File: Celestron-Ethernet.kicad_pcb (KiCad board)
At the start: 4 copper layers, 88.9 x 31.8 mm, 69 parts, among them J1 Joystick, J2 GPS, J3 6P6C, J4 RJ45_Amphenol_RJMG1BD3B8K1ANR, SW1 SW_DIP_x02, SW2 SW_Push, U1 74AHC1G125, U2 ATmega328P-AU, U3 NCV33375ST-3.3, U4 W5500, Y1 8MHz, Y2 25MHz

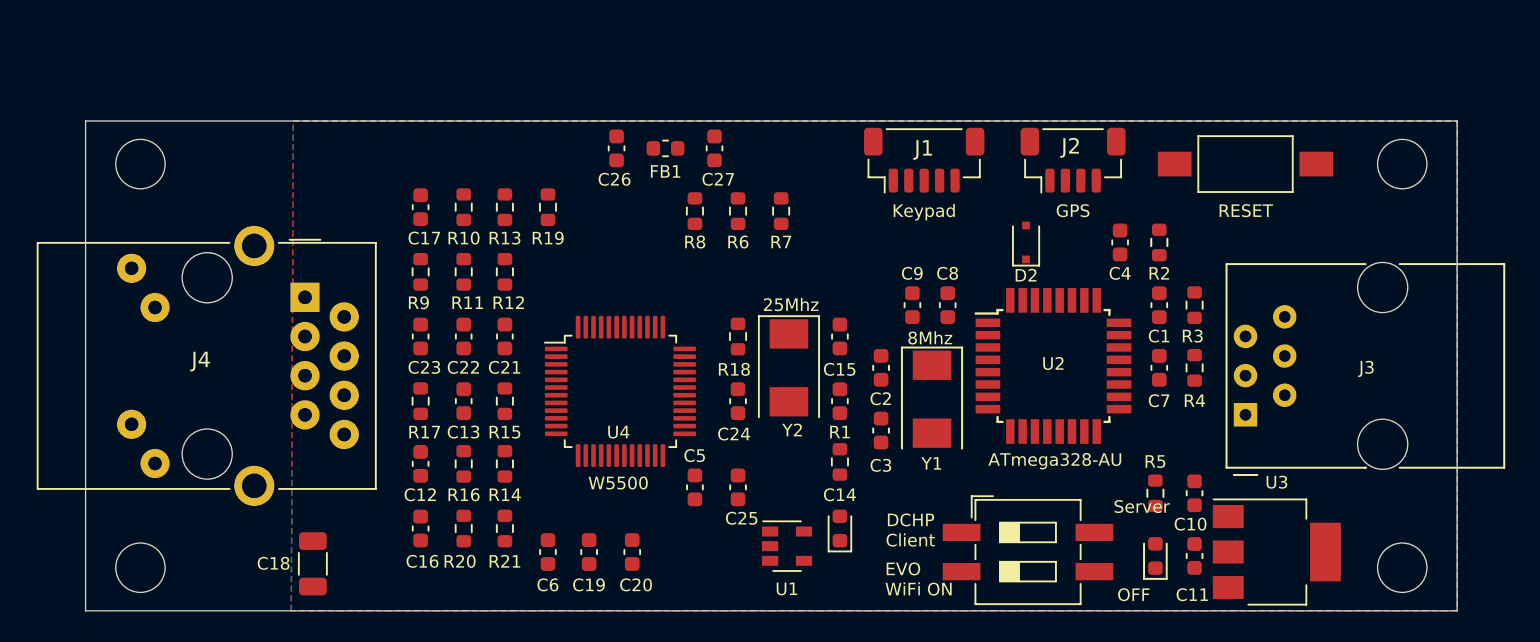
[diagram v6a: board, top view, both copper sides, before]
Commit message: grid spacing
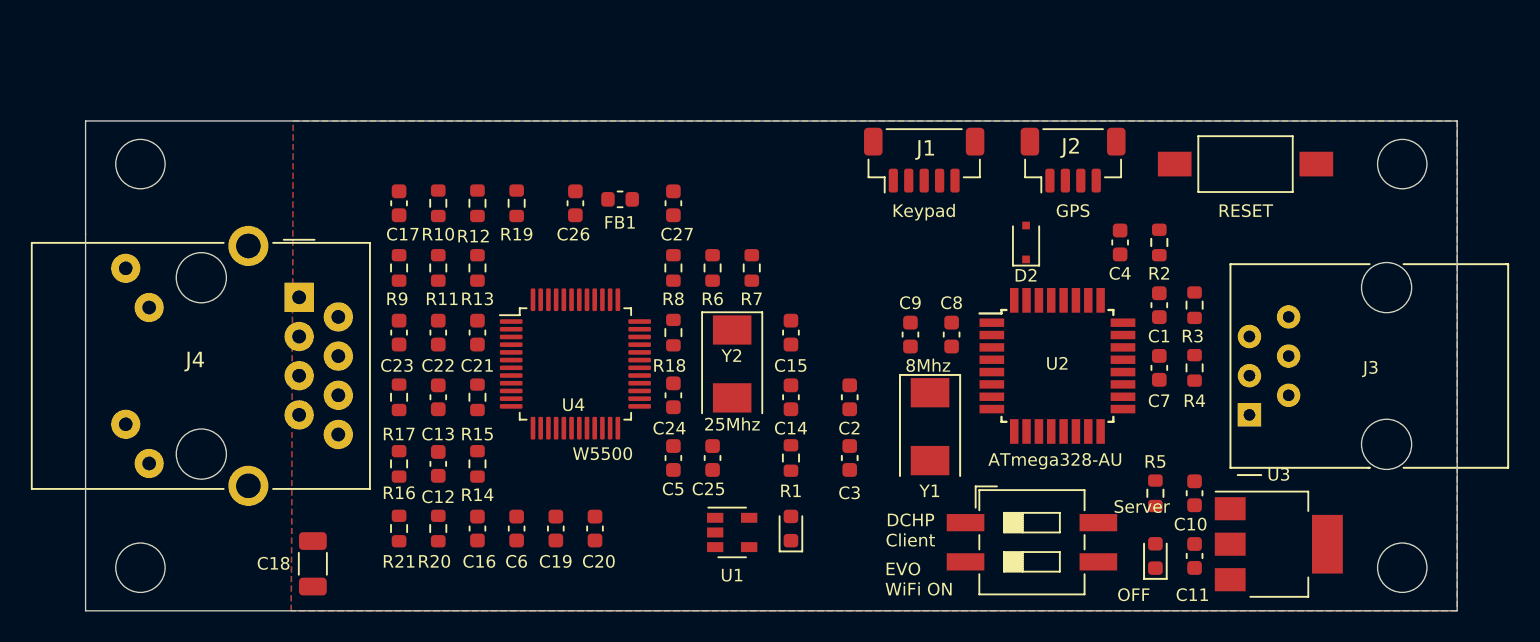
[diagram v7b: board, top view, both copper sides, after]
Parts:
- moved R21 6.86 mm to (121.9, 109.0)
- moved C26 4.44 mm to (133.3, 87.9)
- moved C27 4.44 mm to (139.7, 87.9)
- moved FB1 4.43 mm to (136.2, 87.6)
- moved C24 4.21 mm to (139.7, 100.3)
- moved R18 4.20 mm to (139.7, 96.3)
- moved R16 4.19 mm to (121.9, 104.8), turned to 90 degrees
- moved R7 4.15 mm to (144.8, 92.1)
- moved R6 4.04 mm to (142.2, 92.1)
- moved R8 3.94 mm to (139.7, 92.1)
- moved Y2 3.69 mm to (143.5, 98.3)
- moved C16 3.68 mm to (127.0, 109.0)
- moved U1 3.67 mm to (143.5, 109.2)
- moved U4 3.42 mm to (133.3, 98.3)
- moved C14 3.19 mm to (147.3, 100.5)
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
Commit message: Layout fixed
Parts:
- moved U1 5.26 mm to (148.8, 109.5)
- moved R1 2.57 mm to (144.8, 104.8)
- moved C12 2.54 mm to (121.9, 104.8)
- moved C13 2.54 mm to (121.9, 100.5)
- moved D1 2.54 mm to (144.8, 109.0)
- moved R16 2.54 mm to (124.5, 104.8)
- moved R17 2.54 mm to (124.5, 100.5)
- moved C4 2.25 mm to (170.2, 92.1)
- moved R2 2.25 mm to (172.7, 92.1)
- moved C7 2.16 mm to (170.2, 100.5)
- moved C10 2.05 mm to (172.7, 104.8)
- moved R5 2.05 mm to (170.2, 104.8)
- moved R4 2.05 mm to (172.7, 100.5)
- moved C1 2.05 mm to (170.2, 96.3)
- moved R3 1.93 mm to (172.7, 96.3)
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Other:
- board text removed: "OFF"
- board text removed: "Server"
